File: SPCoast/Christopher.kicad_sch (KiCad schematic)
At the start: 72 parts, among them SW9813 813, SW9815 815, SW9817 817, SW9900 815A, SW9901 813, SW9902 817

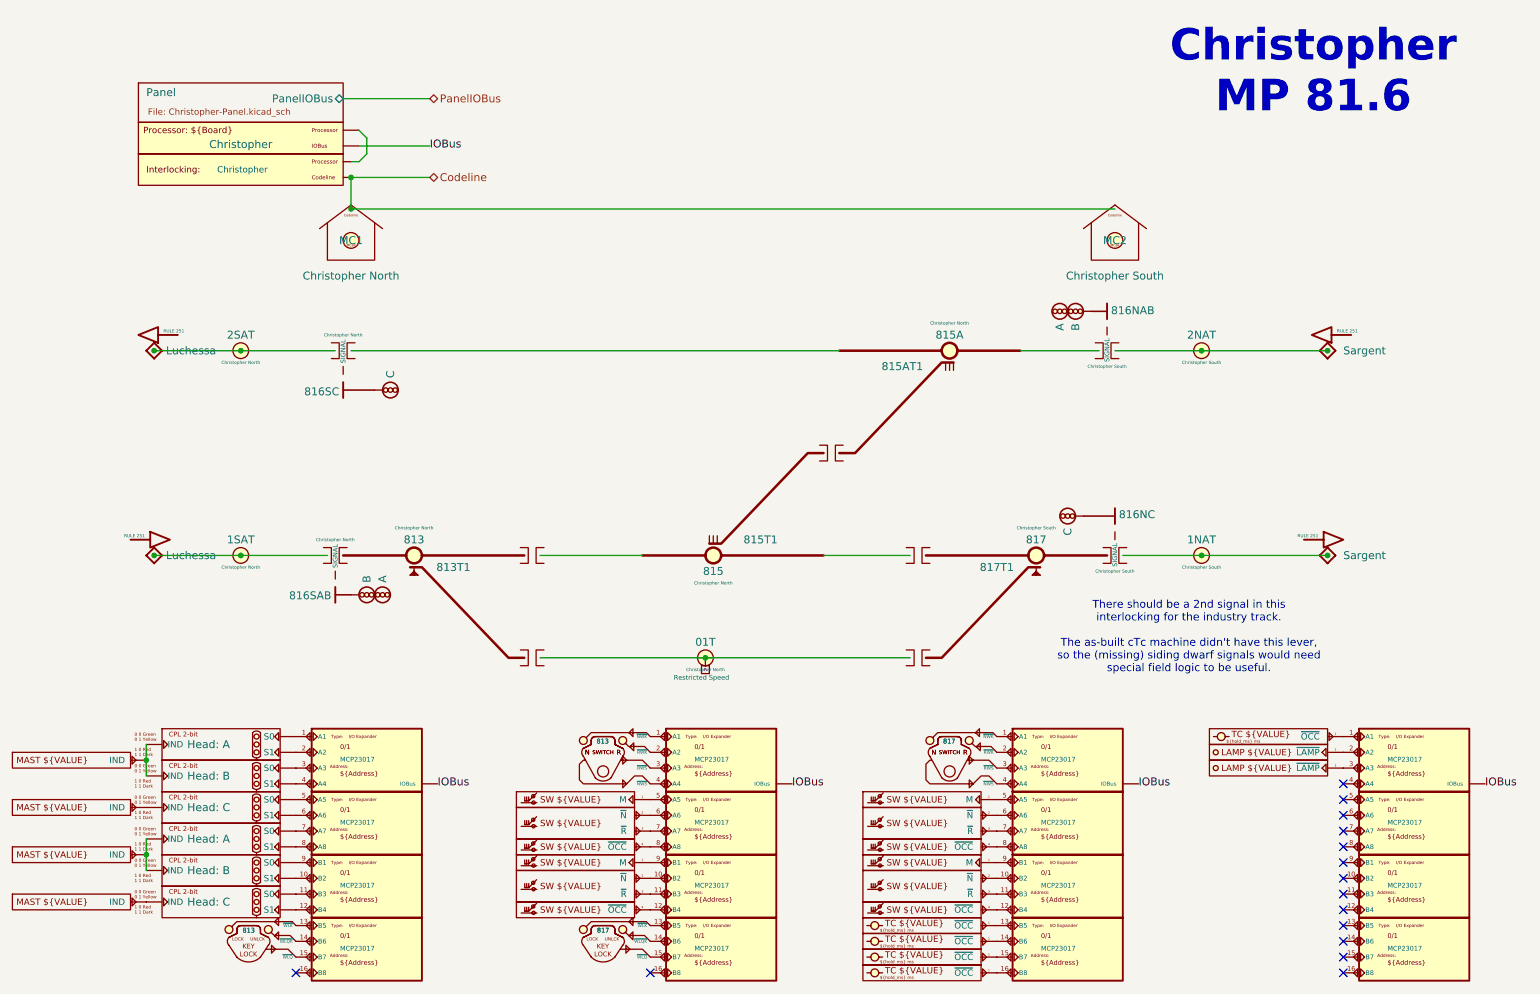
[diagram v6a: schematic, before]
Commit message: feat(kicad): owner edit (2026-10-26): NextCP carries Interlocking; Industry carries Name; HBA leaves the track
The owner's edits after the trackplan review:
- NextCP gains Interlocking = ${Value}, a key the compiler reads for the destination; every instance takes it.
  Christopher's two NextCPs toward Corporal now say Corporal (both said Sargent).
- Industry gains Name = ${VALUE}. The five Industries are named: Gilroy Industry at Luchessa, Beet Loader 1
  and 2 at Corporal and at Sargent.
- Sargent's HBA (hot box alarm) is moved off 1SAT's net; its MC pin is unconnected and it carries Milepost 83.4.
- Watsonville: one Rule 93 (YARD) symbol is moved to the yard side of its joint.
Panels/ is left untracked.

Verified:
- Netlist exported by the owner 2026-10-26 12:37, newer than every sheet and the library.
- lint_symbol_fields: 100 symbols, 0 errors, 0 warnings.

Co-Authored-By: Claude Opus 5.5 <noreply@anthropic.com>
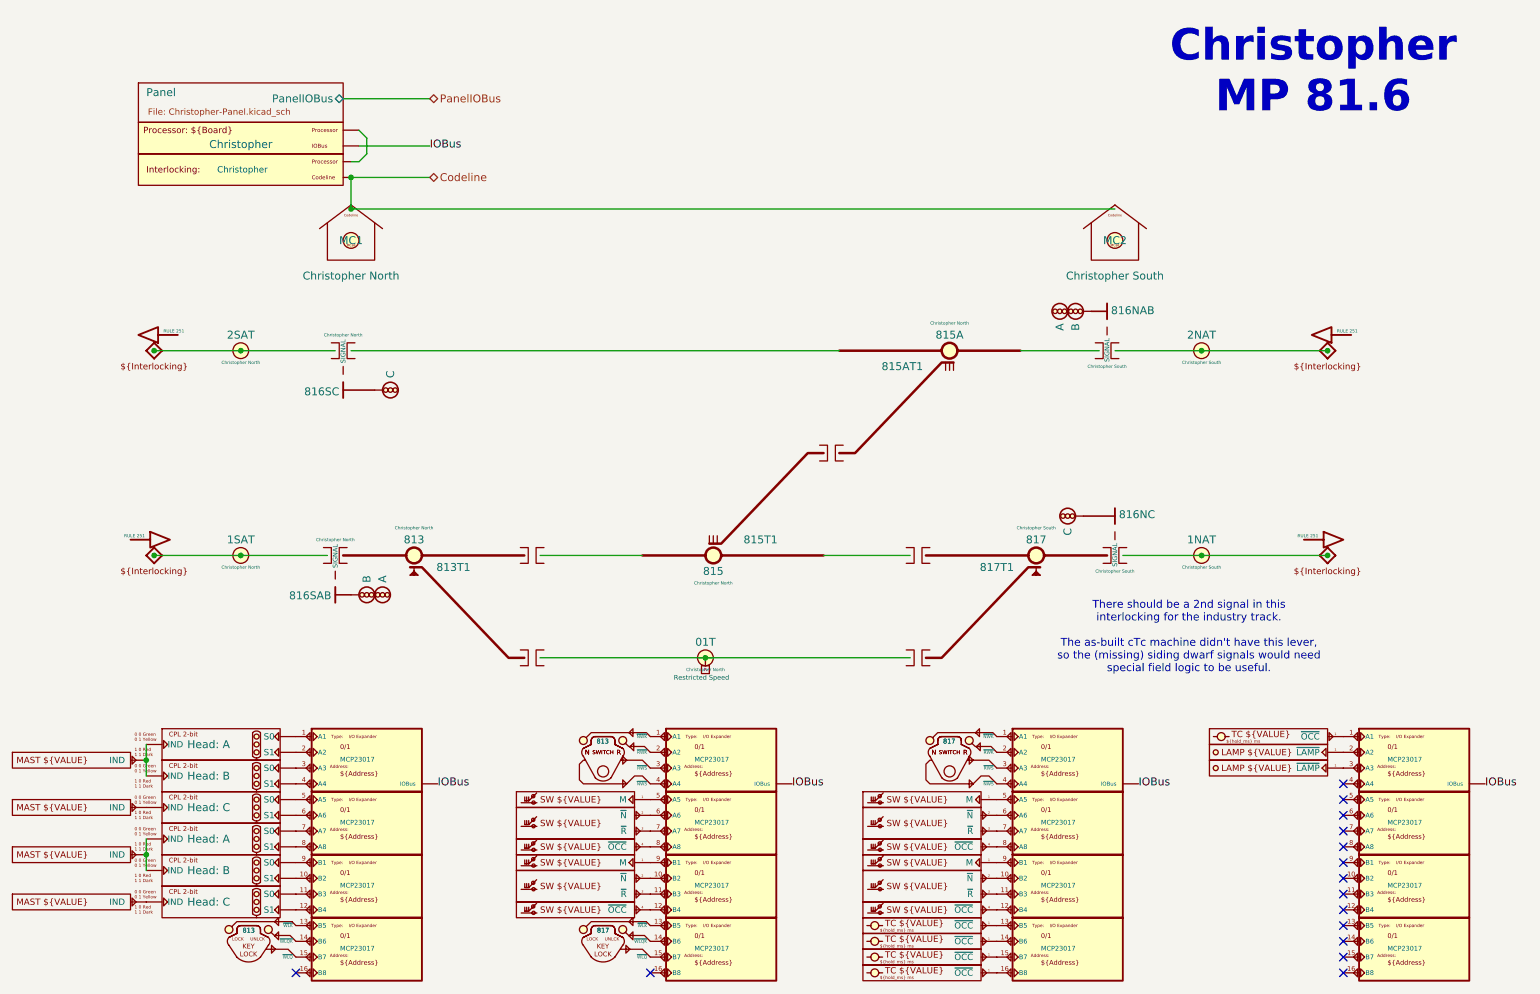
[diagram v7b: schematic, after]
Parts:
- CP9001, CP9002: value Sargent -> Corporal; Interlocking (none) -> ${Value}
- CP9003, CP9004: Interlocking (none) -> ${Value}
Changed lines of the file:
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@@
 	(symbol
 		(lib_id "Railroad-Trackplan:NextCP")
-		(at 41.91 100.33 180)
+		(at 41.91 100.33 0)
 		(unit 1)
 		(body_style 1)
@@
 		(dnp no)
 		(property "Reference" "CP9004"
-			(at 38.735 98.425 0)
+			(at 45.085 102.235 0)
 			(hide yes)
 			(show_name no)
@@
 		)
 		(property "Value" "Luchessa"
-			(at 43.815 100.33 0)
+			(at 44.45 109.22 0)
+			(hide yes)
 			(show_name no)
-			(do_not_autoplace no)
+			(do_not_autoplace yes)
 			(effects
 				(font
@@
 		)
 		(property "Footprint" ""
-			(at 45.72 100.33 0)
+			(at 38.1 100.33 0)
 			(hide yes)
 			(show_name no)
@@
 		)
 		(property "Datasheet" ""
-			(at 45.72 100.33 0)
+			(at 38.1 100.33 0)
 			(hide yes)
 			(show_name no)
@@
 		)
 		(property "Description" "Identifies the next control point on this track"
-			(at 45.085 93.345 0)
+			(at 38.735 107.315 0)
 			(hide yes)
 			(show_name no)
@@
 			)
 		)
+		(property "Interlocking" "${Value}"
+			(at 44.45 109.22 0)
+			(hide yes)
+			(show_name no)
+			(do_not_autoplace no)
+			(effects
+				(font
+					(size 1.27 1.27)
+				)
+			)
+		)
 		(pin "1"
 		)
@@
 	(symbol
 		(lib_id "Railroad-Trackplan:NextCP")
-		(at 231.14 100.33 180)
+		(at 231.14 100.33 0)
 		(unit 1)
 		(body_style 1)
@@
 		(fields_autoplaced yes)
 		(property "Reference" "CP9002"
-			(at 227.965 98.425 0)
+			(at 234.315 102.235 0)
 			(hide yes)
 			(show_name no)
@@
 			)
 		)
-		(property "Value" "Sargent"
-			(at 233.68 100.3299 0)
+		(property "Value" "Corporal"
+			(at 233.68 109.22 0)
+			(hide yes)
 			(show_name no)
-			(do_not_autoplace no)
+			(do_not_autoplace yes)
 			(effects
 				(font
@@
 		)
 		(property "Footprint" ""
-			(at 234.95 100.33 0)
+			(at 227.33 100.33 0)
 			(hide yes)
 			(show_name no)
@@
 		)
 		(property "Datasheet" ""
-			(at 234.95 100.33 0)
+			(at 227.33 100.33 0)
 			(hide yes)
 			(show_name no)
@@
 		)
 		(property "Description" "Identifies the next control point on this track"
-			(at 234.315 93.345 0)
+			(at 227.965 107.315 0)
 			(hide yes)
 			(show_name no)
@@
 			)
 		)
+		(property "Interlocking" "${Value}"
+			(at 233.68 109.22 0)
+			(hide yes)
+			(show_name no)
+			(do_not_autoplace no)
+			(effects
+				(font
+					(size 1.27 1.27)
+				)
+			)
+		)
 		(pin "1"
 		)
@@
 	(symbol
 		(lib_id "Railroad-Trackplan:NextCP")
-		(at 231.14 67.31 180)
+		(at 231.14 67.31 0)
 		(unit 1)
 		(body_style 1)
@@
 		(fields_autoplaced yes)
 		(property "Reference" "CP9001"
-			(at 227.965 65.405 0)
+			(at 234.315 69.215 0)
 			(hide yes)
 			(show_name no)
@@
 			)
 		)
-		(property "Value" "Sargent"
-			(at 233.68 67.3099 0)
+		(property "Value" "Corporal"
+			(at 233.68 76.2 0)
+			(hide yes)
 			(show_name no)
-			(do_not_autoplace no)
+			(do_not_autoplace yes)
 			(effects
 				(font
@@
 		)
 		(property "Footprint" ""
-			(at 234.95 67.31 0)
+			(at 227.33 67.31 0)
 			(hide yes)
 			(show_name no)
@@
 		)
 		(property "Datasheet" ""
-			(at 234.95 67.31 0)
+			(at 227.33 67.31 0)
 			(hide yes)
 			(show_name no)
@@
 		)
 		(property "Description" "Identifies the next control point on this track"
-			(at 234.315 60.325 0)
+			(at 227.965 74.295 0)
 			(hide yes)
 			(show_name no)
@@
 			)
 		)
+		(property "Interlocking" "${Value}"
+			(at 233.68 76.2 0)
+			(hide yes)
+			(show_name no)
+			(do_not_autoplace no)
+			(effects
+				(font
+					(size 1.27 1.27)
+				)
+			)
+		)
 		(pin "1"
 		)
@@
 	(symbol
 		(lib_id "Railroad-Trackplan:NextCP")
-		(at 41.91 67.31 180)
+		(at 41.91 67.31 0)
 		(unit 1)
 		(body_style 1)
@@
 		(dnp no)
 		(property "Reference" "CP9003"
-			(at 38.735 65.405 0)
+			(at 45.085 69.215 0)
 			(hide yes)
 			(show_name no)
@@
 		)
 		(property "Value" "Luchessa"
-			(at 43.815 67.31 0)
+			(at 44.45 76.2 0)
+			(hide yes)
 			(show_name no)
-			(do_not_autoplace no)
+			(do_not_autoplace yes)
 			(effects
 				(font
@@
 		)
 		(property "Footprint" ""
-			(at 45.72 67.31 0)
+			(at 38.1 67.31 0)
 			(hide yes)
 			(show_name no)
@@
 		)
 		(property "Datasheet" ""
-			(at 45.72 67.31 0)
+			(at 38.1 67.31 0)
 			(hide yes)
 			(show_name no)
@@
 		)
 		(property "Description" "Identifies the next control point on this track"
-			(at 45.085 60.325 0)
+			(at 38.735 74.295 0)
 			(hide yes)
 			(show_name no)
@@
 			(hide yes)
 			(show_name no)
+			(do_not_autoplace no)
+			(effects
+				(font
+					(size 1.27 1.27)
+				)
+			)
+		)
+		(property "Interlocking" "${Value}"
+			(at 44.45 76.2 0)
+			(hide yes)
+			(show_name no)
